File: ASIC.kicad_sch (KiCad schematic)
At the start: 2 parts, among them U3 BM1370_mode1, U4 BM1370_mode1

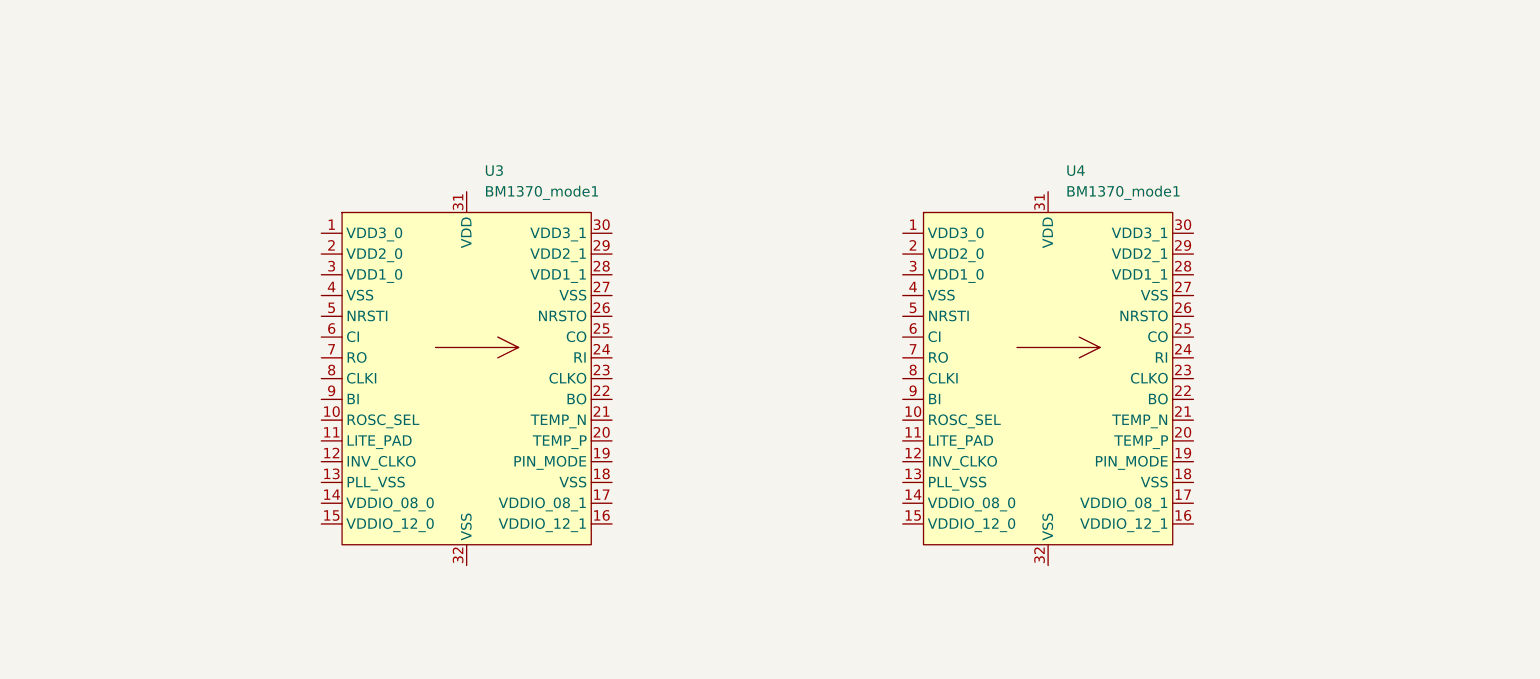
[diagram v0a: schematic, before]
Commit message: More schematic work for ASICs and ESP32
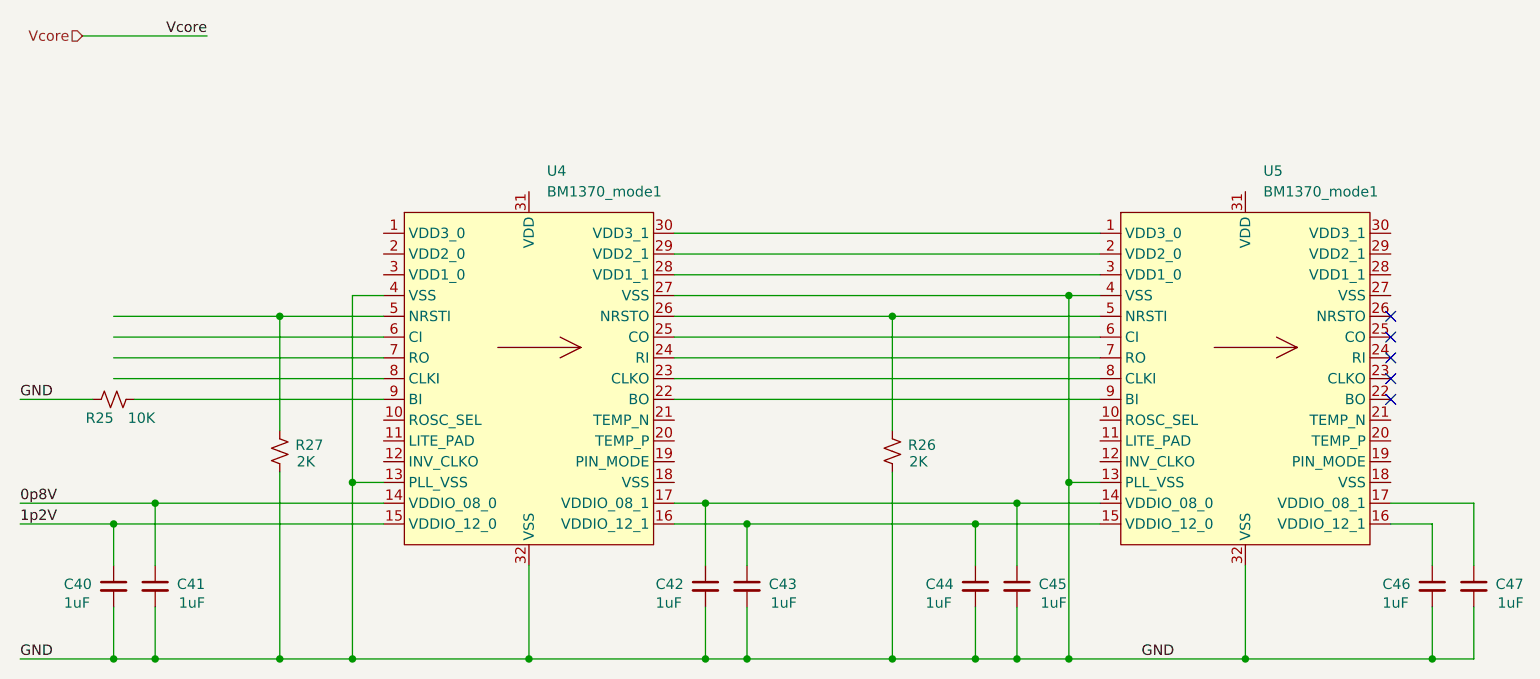
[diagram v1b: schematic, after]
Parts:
- added C40, C41, C42, C43, C44, C45, C46, C47: 1uF, symbol Device:C_Small
- added R25: 10K, symbol Device:R_Small_US
- added R26, R27: 2K, symbol Device:R_Small_US
- renumbered U3 to U4, U4 to U5
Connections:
- net at U5.1 (VDD3_0): now also U4.30 (VDD3_1)
- net GND: now reaches U5.13 (PLL_VSS)
- net GND: now also U4.13 (PLL_VSS), U4.27 (VSS), U4.32 (VSS), U4.4 (VSS), U5.32 (VSS), U5.4 (VSS), C40.2, C41.2, C42.2, C43.2, C44.2, C45.2, C46.2, C47.2, R25.1, R26.1, R27.1
- net at U5.14 (VDDIO_08_0): now also U4.17 (VDDIO_08_1), C42.1, C45.1
- net at U5.15 (VDDIO_12_0): now also U4.16 (VDDIO_12_1), C43.1, C44.1
- net at U5.16 (VDDIO_12_1): now also C46.1
- net at U5.17 (VDDIO_08_1): now also C47.1
- net at U5.2 (VDD2_0): now also U4.29 (VDD2_1)
- net at U5.3 (VDD1_0): now also U4.28 (VDD1_1)
- net at U5.5 (NRSTI): now also U4.26 (NRSTO), R26.2
- net at U5.6 (CI): now also U4.25 (CO)
- net at U5.7 (RO): now also U4.24 (RI)
- net at U5.8 (CLKI): now also U4.23 (CLKO)
- net at U5.9 (BI): now also U4.22 (BO)
- net 0p8V: now reaches U4.14 (VDDIO_08_0)
- net 0p8V: now also C41.1
- net 1p2V: now reaches U4.15 (VDDIO_12_0)
- net 1p2V: now also C40.1
- net at U4.5 (NRSTI): now also R27.2
- net at U4.9 (BI): now also R25.2
- no-connect marks 0 -> 5
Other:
- moved on the sheet: U4, U5

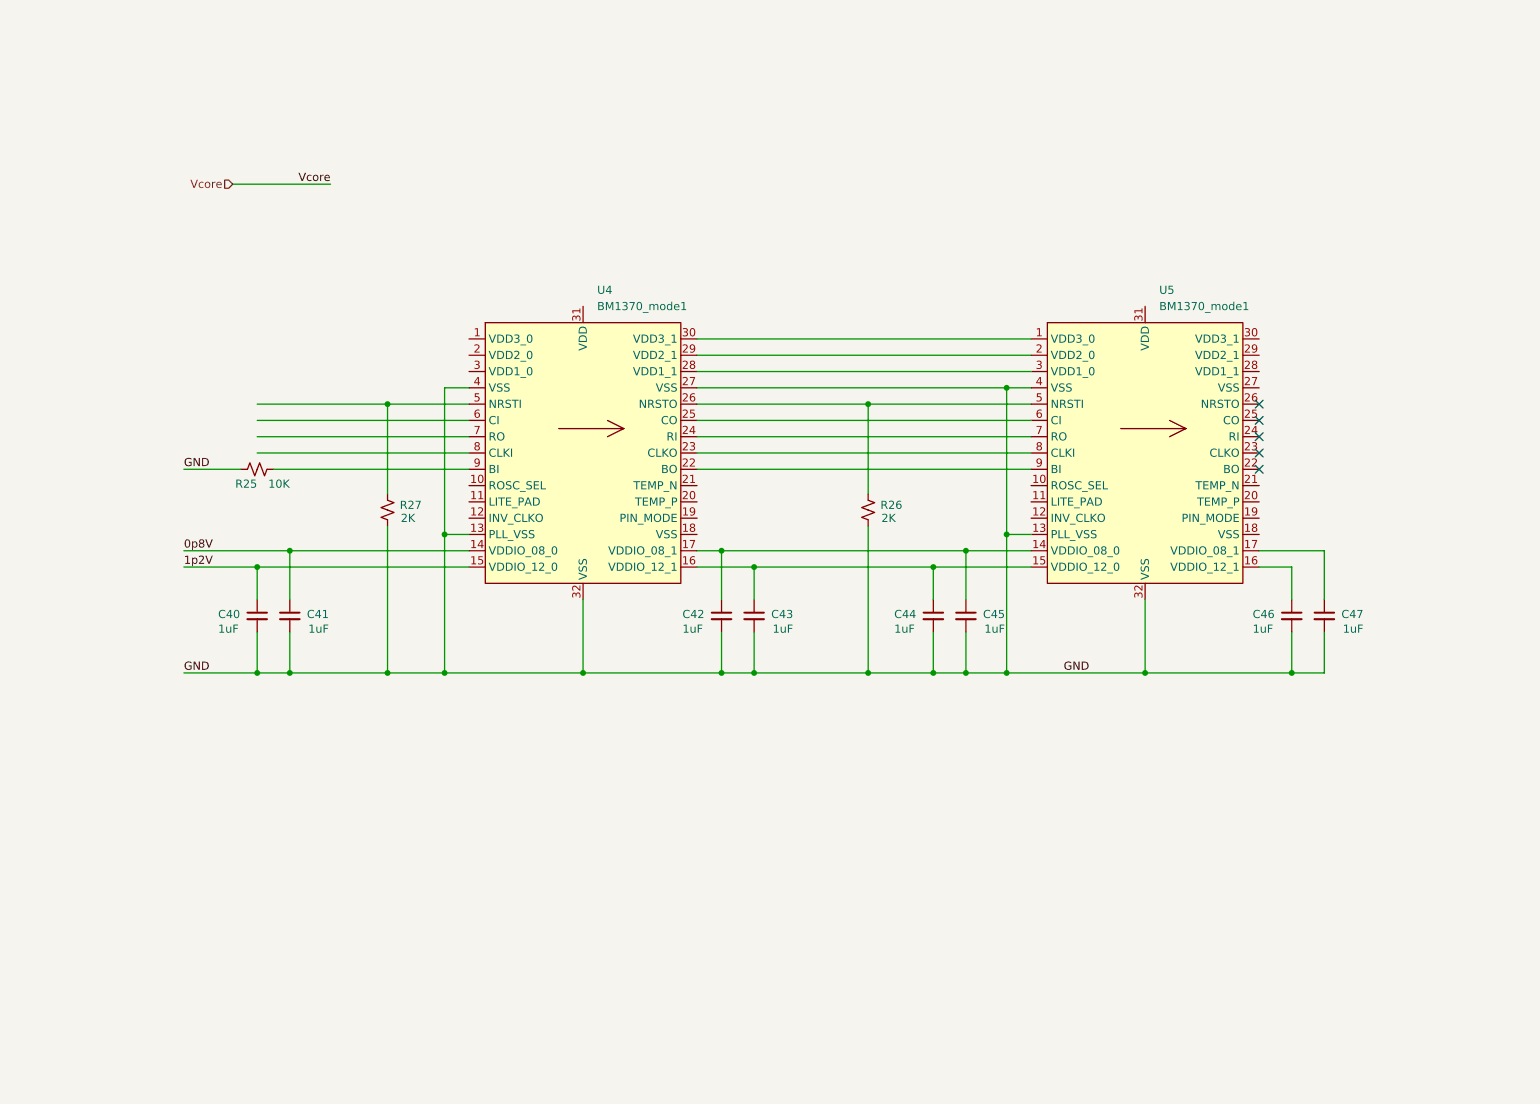
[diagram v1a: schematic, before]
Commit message: Finish wiring ASICs and ESP32
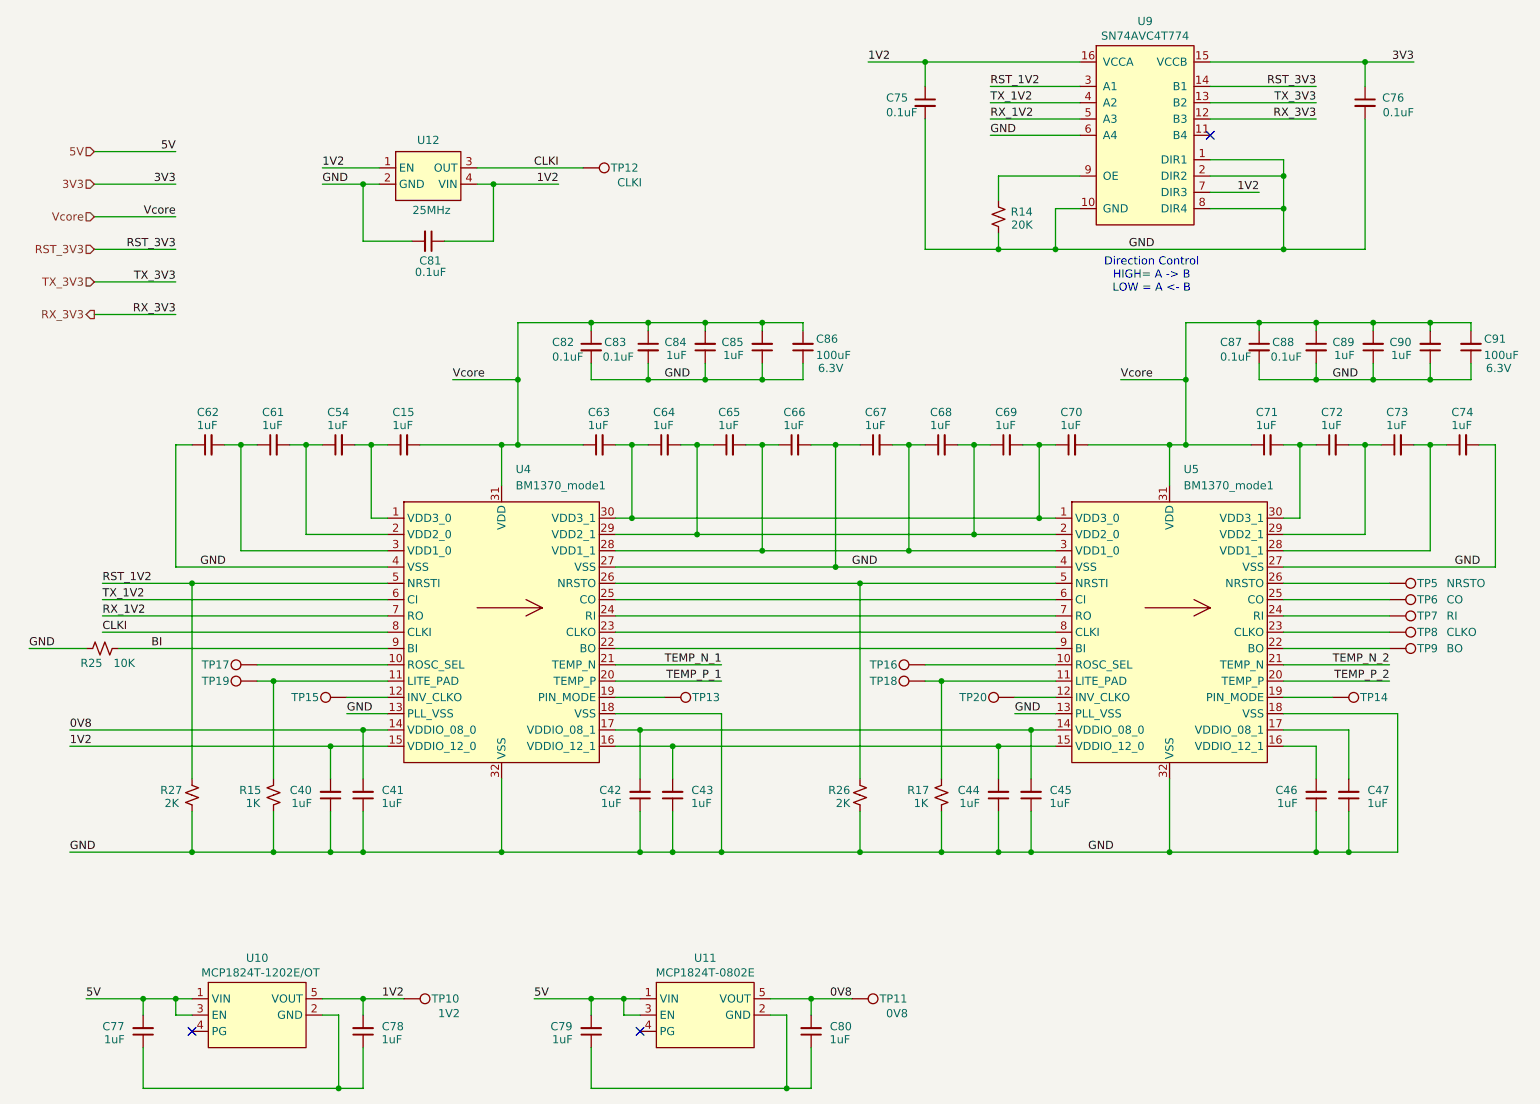
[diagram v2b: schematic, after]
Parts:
- added C15, C54, C61, C62, C63, C64, C65, C66, C67, C68, C69, C70, C71, C72, C73, C74, C77, C78, C79, C80, C84, C85, C89, C90: 1uF, Capacitor_SMD:C_0402_1005Metric, symbol Device:C_Small
- added C75, C76, C81, C82, C83, C87, C88: 0.1uF, Capacitor_SMD:C_0402_1005Metric, symbol Device:C_Small
- added C86, C91: 100uF, Capacitor_SMD:C_1210_3225Metric, symbol Device:C_Small
- added R14: 20K, symbol Device:R_Small_US
- added R15, R17: 1K, symbol Device:R_Small_US
- added TP10: 1V2, symbol Connector:TestPoint
- added TP11: 0V8, symbol Connector:TestPoint
- added TP12: CLKI, symbol Connector:TestPoint
- added TP13, TP14: PM1, symbol Connector:TestPoint
- added TP15, TP16, TP17, TP18, TP19, TP20: INV_CLKO, symbol Connector:TestPoint
- added TP5: NRSTO, symbol Connector:TestPoint
- added TP6: CO, symbol Connector:TestPoint
- added TP7: RI, symbol Connector:TestPoint
- added TP8: CLKO, symbol Connector:TestPoint
- added TP9: BO, symbol Connector:TestPoint
- added U10: MCP1824T-1202E/OT, Package_TO_SOT_SMD:SOT-23-5, symbol bitaxe:MCP1824
- added U11: MCP1824T-0802E, Package_TO_SOT_SMD:SOT-23-5, symbol bitaxe:MCP1824
- added U12: 25MHz, symbol bitaxe:oscillator
- added U9: SN74AVC4T774, Package_SO:TSSOP-16_4.4x5mm_P0.65mm, symbol bitaxe:SN74AVC4T774
- C40, C41, C42, C43, C44, C45, C46, C47: footprint (none) -> Capacitor_SMD:C_0402_1005Metric; DK (none) -> 587-5514-1-ND; PARTNUM (none) -> EMK105BJ105MV-F
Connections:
- net GND: now also C40.1, C41.1, C42.1, C43.1, C44.1, C45.1, C46.1, C47.1, U4.18 (VSS), U5.18 (VSS), U5.27 (VSS), C62.1, C66.2, C67.1, C74.2, C75.2, C76.2, C81.2, C82.2, C83.2, C84.1, C85.1, C86.1, C87.2, C88.2, C89.1, C90.1, C91.1, R14.1, R15.1, R17.1, U12.2 (GND), U9.1 (DIR1), U9.10 (GND), U9.2 (DIR2), U9.6 (A4), U9.8 (DIR4); no longer C40.2, C41.2, C42.2, C43.2, C44.2, C45.2, C46.2, C47.2
- net Vcore: now also U4.31 (VDD), U5.31 (VDD), C15.2, C63.1, C70.2, C71.1, C82.1, C83.1, C84.2, C85.2, C86.2, C87.1, C88.1, C89.2, C90.2, C91.2
- net RST_1V2: now reaches R27.2, U4.5 (NRSTI)
- net RST_1V2: now also U9.3 (A1)
- net at U4.30 (VDD3_1), U5.1 (VDD3_0): now also C63.2, C64.1, C69.2, C70.1
- net at U5.10 (ROSC_SEL): now also TP16.1
- net at U5.11 (LITE_PAD): now also R17.2, TP18.1
- net at U5.12 (INV_CLKO): now also TP20.1
- net at U4.17 (VDDIO_08_1), U5.14 (VDDIO_08_0): now also C42.2, C45.2; no longer C42.1, C45.1
- net at U4.16 (VDDIO_12_1), U5.15 (VDDIO_12_0): now also C43.2, C44.2; no longer C43.1, C44.1
- net at U5.16 (VDDIO_12_1): now also C46.2; no longer C46.1
- net at U5.17 (VDDIO_08_1): now also C47.2; no longer C47.1
- net at U5.19 (PIN_MODE): now also TP14.1
- net at U4.29 (VDD2_1), U5.2 (VDD2_0): now also C64.2, C65.1, C68.2, C69.1
- net TEMP_P_2: now reaches U5.20 (TEMP_P)
- net TEMP_N_2: now reaches U5.21 (TEMP_N)
- net at U5.22 (BO): now also TP9.1
- net at U5.23 (CLKO): now also TP8.1
- net at U5.24 (RI): now also TP7.1
- net at U5.25 (CO): now also TP6.1
- net at U5.26 (NRSTO): now also TP5.1
- net at U5.28 (VDD1_1): now also C73.2, C74.1
- net at U5.29 (VDD2_1): now also C72.2, C73.1
- net at U4.28 (VDD1_1), U5.3 (VDD1_0): now also C65.2, C66.1, C67.2, C68.1
- net at U5.30 (VDD3_1): now also C71.2, C72.1
- net at U4.1 (VDD3_0): now also C15.1, C54.2
- net at U4.10 (ROSC_SEL): now also TP17.1
- net at U4.11 (LITE_PAD): now also R15.2, TP19.1
- net at U4.12 (INV_CLKO): now also TP15.1
- net at U4.19 (PIN_MODE): now also TP13.1
- net at U4.2 (VDD2_0): now also C54.1, C61.2
- net TEMP_P_1: now reaches U4.20 (TEMP_P)
- net TEMP_N_1: now reaches U4.21 (TEMP_N)
- net at U4.3 (VDD1_0): now also C61.1, C62.2
- net TX_1V2: now reaches U4.6 (CI)
- net TX_1V2: now also U9.4 (A2)
- net RX_1V2: now reaches U4.7 (RO)
- net RX_1V2: now also U9.5 (A3)
- net CLKI: now reaches U4.8 (CLKI)
- net CLKI: now also TP12.1, U12.3 (OUT)
- net BI: now reaches R25.2, U4.9 (BI)
- net 0p8V renamed 0V8
- net 0V8: now also C41.2, C80.2, TP11.1, U11.5 (VOUT); no longer C41.1
- net 1p2V renamed 1V2
- net 1V2: now also C40.2, C75.1, C78.2, C81.1, TP10.1, U10.5 (VOUT), U12.1 (EN), U12.4 (VIN), U9.16 (VCCA), U9.7 (DIR3); no longer C40.1
- new net: C79.1, C80.1, U11.2 (GND)
- new net: C77.1, C78.1, U10.2 (GND)
- new net: R14.2, U9.9 (OE)
- new net 3V3: C76.1, U9.15 (VCCB)
- new net 5V: C77.2, C79.2, U10.1 (VIN), U10.3 (EN), U11.1 (VIN), U11.3 (EN)
- new net RST_3V3: U9.14 (B1)
- new net RX_3V3: U9.12 (B3)
- new net TX_3V3: U9.13 (B2)
- no-connect marks 5 -> 3
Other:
- note added: "Direction Control HIGH= A -> B LOW = A <- B"
- moved on the sheet: R25, R26, R27, U4, U5

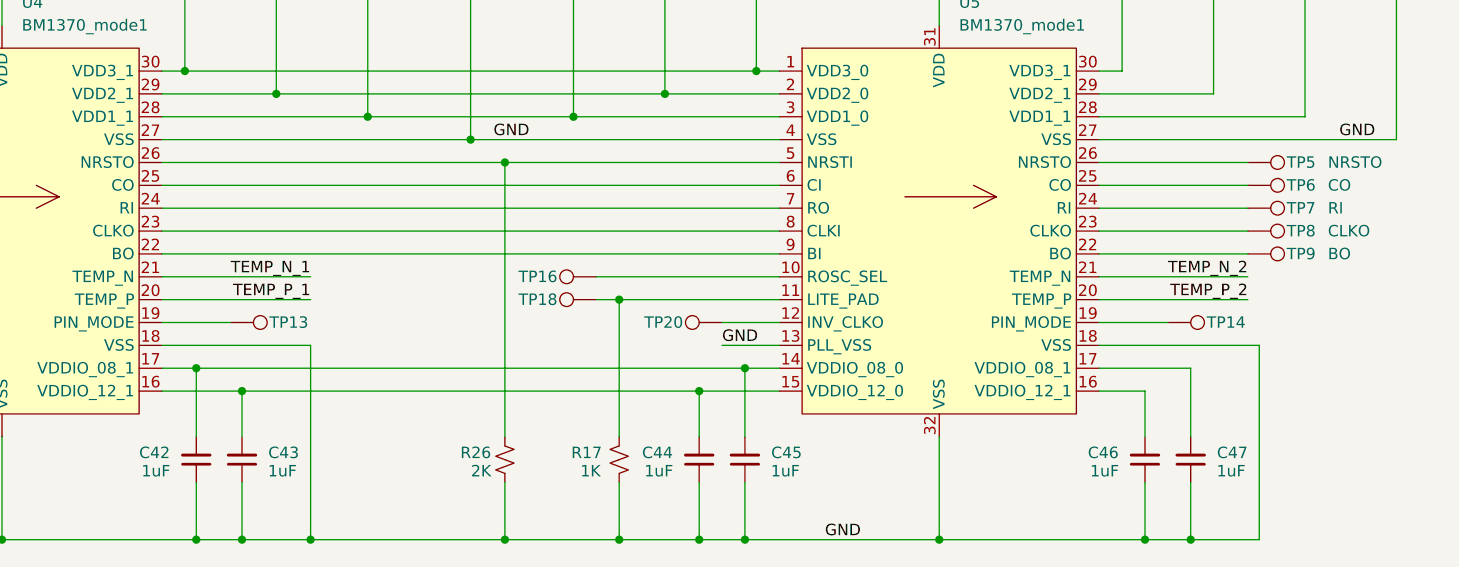
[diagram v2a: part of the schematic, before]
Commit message: add fan chip
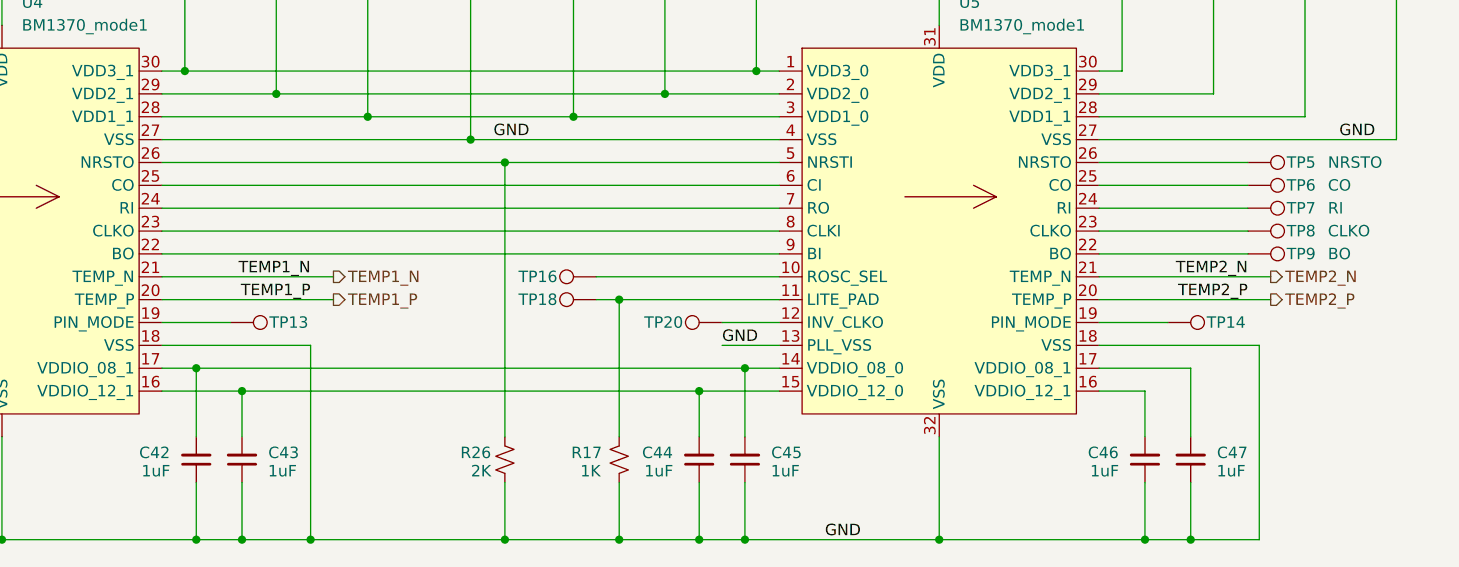
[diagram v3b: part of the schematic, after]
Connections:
- net TEMP_N_1 renamed TEMP1_N
- net TEMP_N_2 renamed TEMP2_N
- net TEMP_P_1 renamed TEMP1_P
- net TEMP_P_2 renamed TEMP2_P
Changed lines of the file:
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@@
 	(wire
 		(pts
-			(xy 217.17 124.46) (xy 233.68 124.46)
-		)
-		(stroke
-			(width 0)
-			(type default)
-		)
-	)
-	(wire
-		(pts
-			(xy 113.03 124.46) (xy 129.54 124.46)
+			(xy 217.17 124.46) (xy 236.22 124.46)
+		)
+		(stroke
+			(width 0)
+			(type default)
+		)
+	)
+	(wire
+		(pts
+			(xy 113.03 124.46) (xy 132.08 124.46)
 		)
 		(stroke
@@
 	(wire
 		(pts
-			(xy 217.17 121.92) (xy 233.68 121.92)
+			(xy 217.17 121.92) (xy 236.22 121.92)
 		)
 		(stroke
@@
 	(wire
 		(pts
-			(xy 113.03 121.92) (xy 129.54 121.92)
+			(xy 113.03 121.92) (xy 132.08 121.92)
 		)
 		(stroke
@@
 		)
 	)
-	(label "TEMP_N_2"
+	(label "TEMP2_N"
 		(at 233.68 121.92 180)
 		(fields_autoplaced yes)
@@
 		)
 	)
-	(label "TEMP_N_1"
+	(label "TEMP1_N"
 		(at 129.54 121.92 180)
 		(fields_autoplaced yes)
@@
 		)
 	)
-	(label "TEMP_P_1"
+	(label "TEMP1_P"
 		(at 129.54 124.46 180)
 		(fields_autoplaced yes)
@@
 		)
 	)
-	(label "TEMP_P_2"
+	(label "TEMP2_P"
 		(at 233.68 124.46 180)
 		(fields_autoplaced yes)
@@
 		)
 	)
+	(hierarchical_label "TEMP1_P"
+		(shape output)
+		(at 132.08 124.46 0)
+		(fields_autoplaced yes)
+		(effects
+			(font
+				(size 1.27 1.27)
+			)
+			(justify left)
+		)
+	)
 	(hierarchical_label "RX_3V3"
 		(shape output)
@@
 		)
 	)
+	(hierarchical_label "TEMP1_N"
+		(shape output)
+		(at 132.08 121.92 0)
+		(fields_autoplaced yes)
+		(effects
+			(font
+				(size 1.27 1.27)
+			)
+			(justify left)
+		)
+	)
 	(hierarchical_label "5V"
 		(shape input)
@@
 		)
 	)
+	(hierarchical_label "TEMP2_N"
+		(shape output)
+		(at 236.22 121.92 0)
+		(fields_autoplaced yes)
+		(effects
+			(font
+				(size 1.27 1.27)
+			)
+			(justify left)
+		)
+	)
+	(hierarchical_label "TEMP2_P"
+		(shape output)
+		(at 236.22 124.46 0)
+		(fields_autoplaced yes)
+		(effects
+			(font
+				(size 1.27 1.27)
+			)
+			(justify left)
+		)
+	)
